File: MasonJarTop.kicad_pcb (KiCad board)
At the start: 2 copper layers, 65.6 x 65.6 mm, 17 parts, among them P1 CONN_01X02, P2 Loop Mounting Hole, P3 Loop Mounting Hole

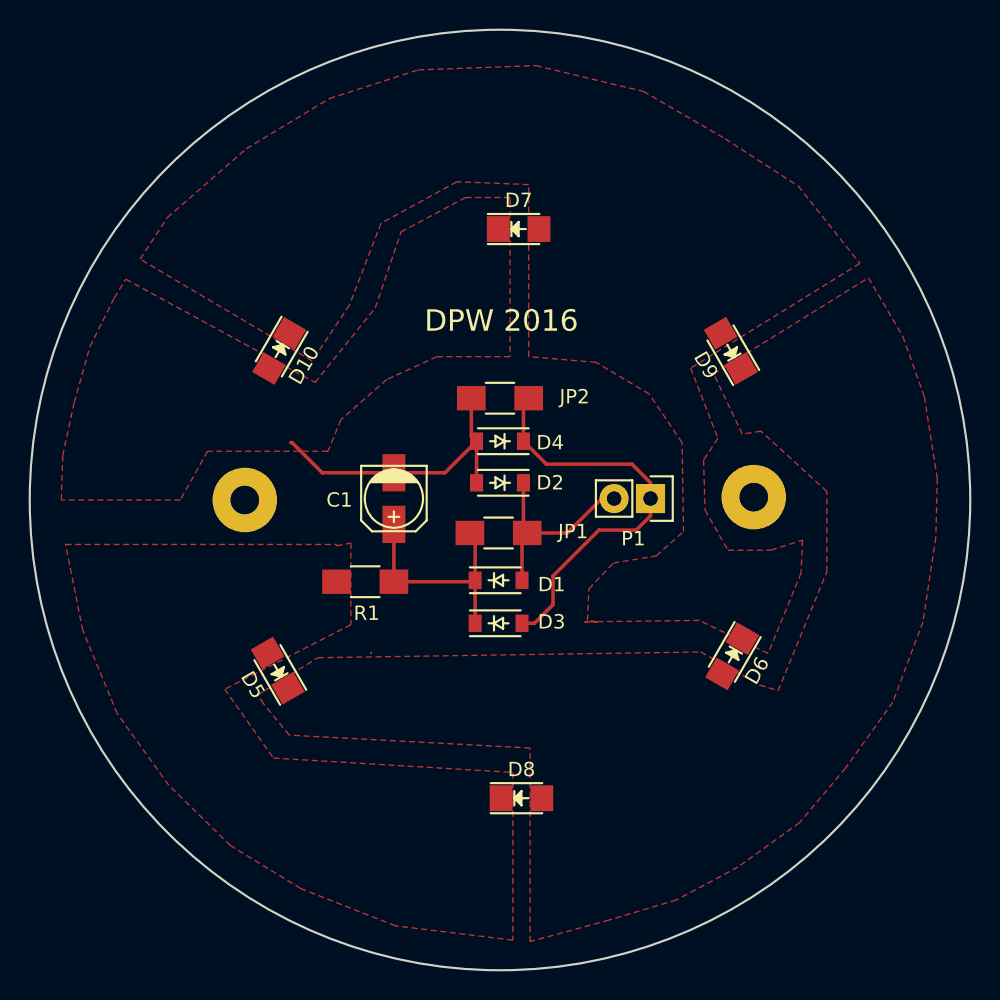
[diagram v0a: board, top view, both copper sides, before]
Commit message: Modify schematic after testing and re-layout complete.
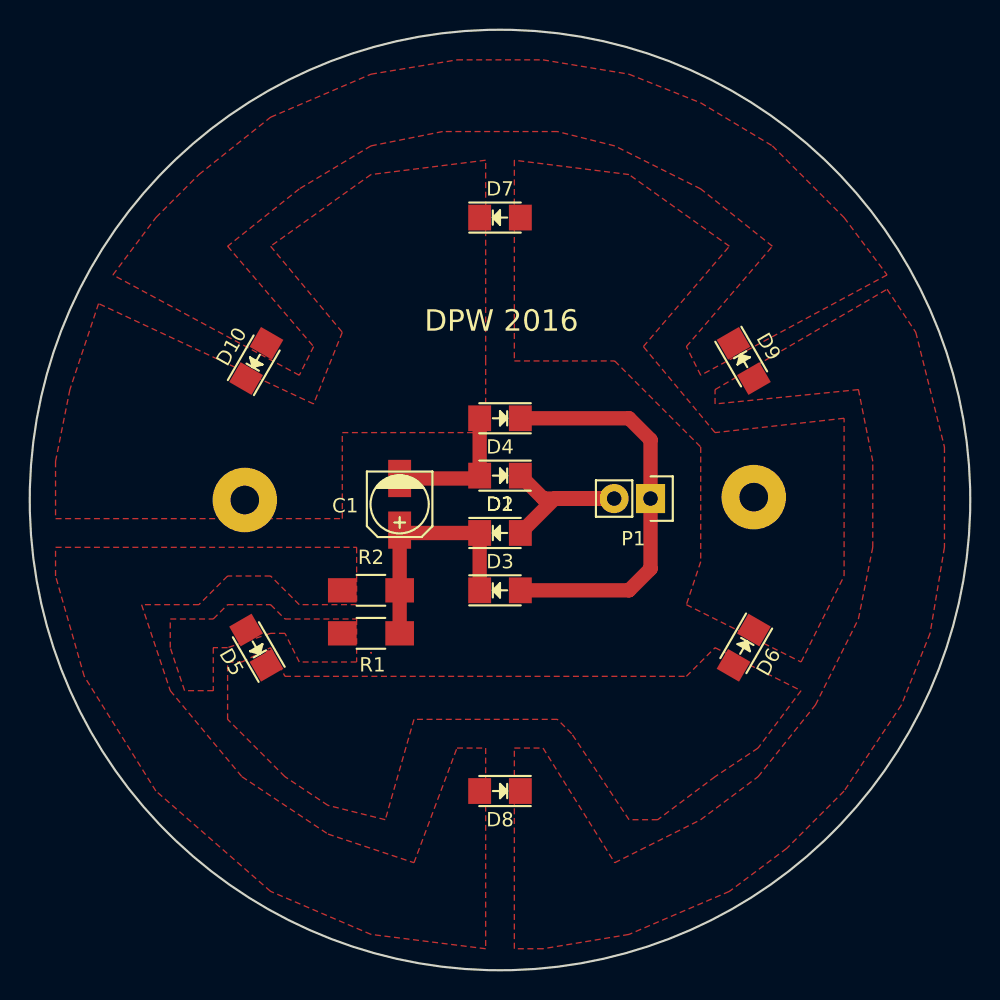
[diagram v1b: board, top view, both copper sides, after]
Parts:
- removed JP1, JP2: 0.0, Resistors_SMD:R_1206_HandSoldering
- added R2: 56, Resistors_SMD:R_1206_HandSoldering, F.Cu at (114.0, 115.0)
- D1, D2, D3, D4: footprint Diodes_SMD:SOD-123 -> LEDs:LED_1206
- R1: value 20 -> 56
- moved R1 3.62 mm to (114.0, 118.0)
- moved D1 3.30 mm to (123.0, 111.0)
- moved D3 2.30 mm to (123.0, 115.0)
- moved D5 2.19 mm to (106.0, 119.0)
- moved D10 1.75 mm to (106.0, 99.0), turned to 60 degrees
- moved D4 1.60 mm to (123.0, 103.0)
- moved D8 1.58 mm to (123.0, 129.0), turned to 180 degrees
- moved D7 1.53 mm to (123.0, 89.0)
- moved D9 1.14 mm to (140.0, 99.0), turned to 300 degrees
- moved D6 1.00 mm to (140.0, 119.0)
- moved C1 0.57 mm to (116.0, 109.0)
- moved D2 0.50 mm to (123.0, 107.0)
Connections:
- D10 pad 1: Net-(D10-Pad1) -> Net-(C1-Pad2)
- D10 pad 2: Net-(C1-Pad2) -> Net-(D10-Pad2)
- D6 pad 1: Net-(D10-Pad1) -> Net-(D6-Pad1)
- D7 pad 2: Net-(D10-Pad1) -> Net-(D6-Pad1)
- D8 pad 1: Net-(D5-Pad2) -> Net-(D8-Pad1)
- D8 pad 2: Net-(D5-Pad1) -> Net-(D8-Pad2)
- D9 pad 1: Net-(D5-Pad1) -> Net-(D10-Pad2)
- D9 pad 2: Net-(D10-Pad1) -> Net-(D8-Pad1)
- P2 pad 1: Net-(P2-Pad1) -> (no net)
- P3 pad 1: Net-(P3-Pad1) -> (no net)
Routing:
- net Net-(C1-Pad2): track 20.8 -> 9.66 mm
- net Net-(D1-Pad2): track 13.9 -> 15.6 mm
- net Net-(C1-Pad1): track 16.2 -> 17.0 mm
- added copper zone on F.Cu, net Net-(D10-Pad2)
- added copper zone on F.Cu, net Net-(D6-Pad1)
- added copper zone on F.Cu, net Net-(D8-Pad1)
- added copper zone on F.Cu, net Net-(D8-Pad2)
- removed copper zone on F.Cu, net Net-(D10-Pad1)
